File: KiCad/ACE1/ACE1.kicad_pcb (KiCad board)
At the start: 2 copper layers, 198.2 x 224.3 mm, 148 parts, among them IC1 78T, Q1 2N3904, Q2 2N2369, Q3 BC183, Q4 2N3904, X1 6.556MHz

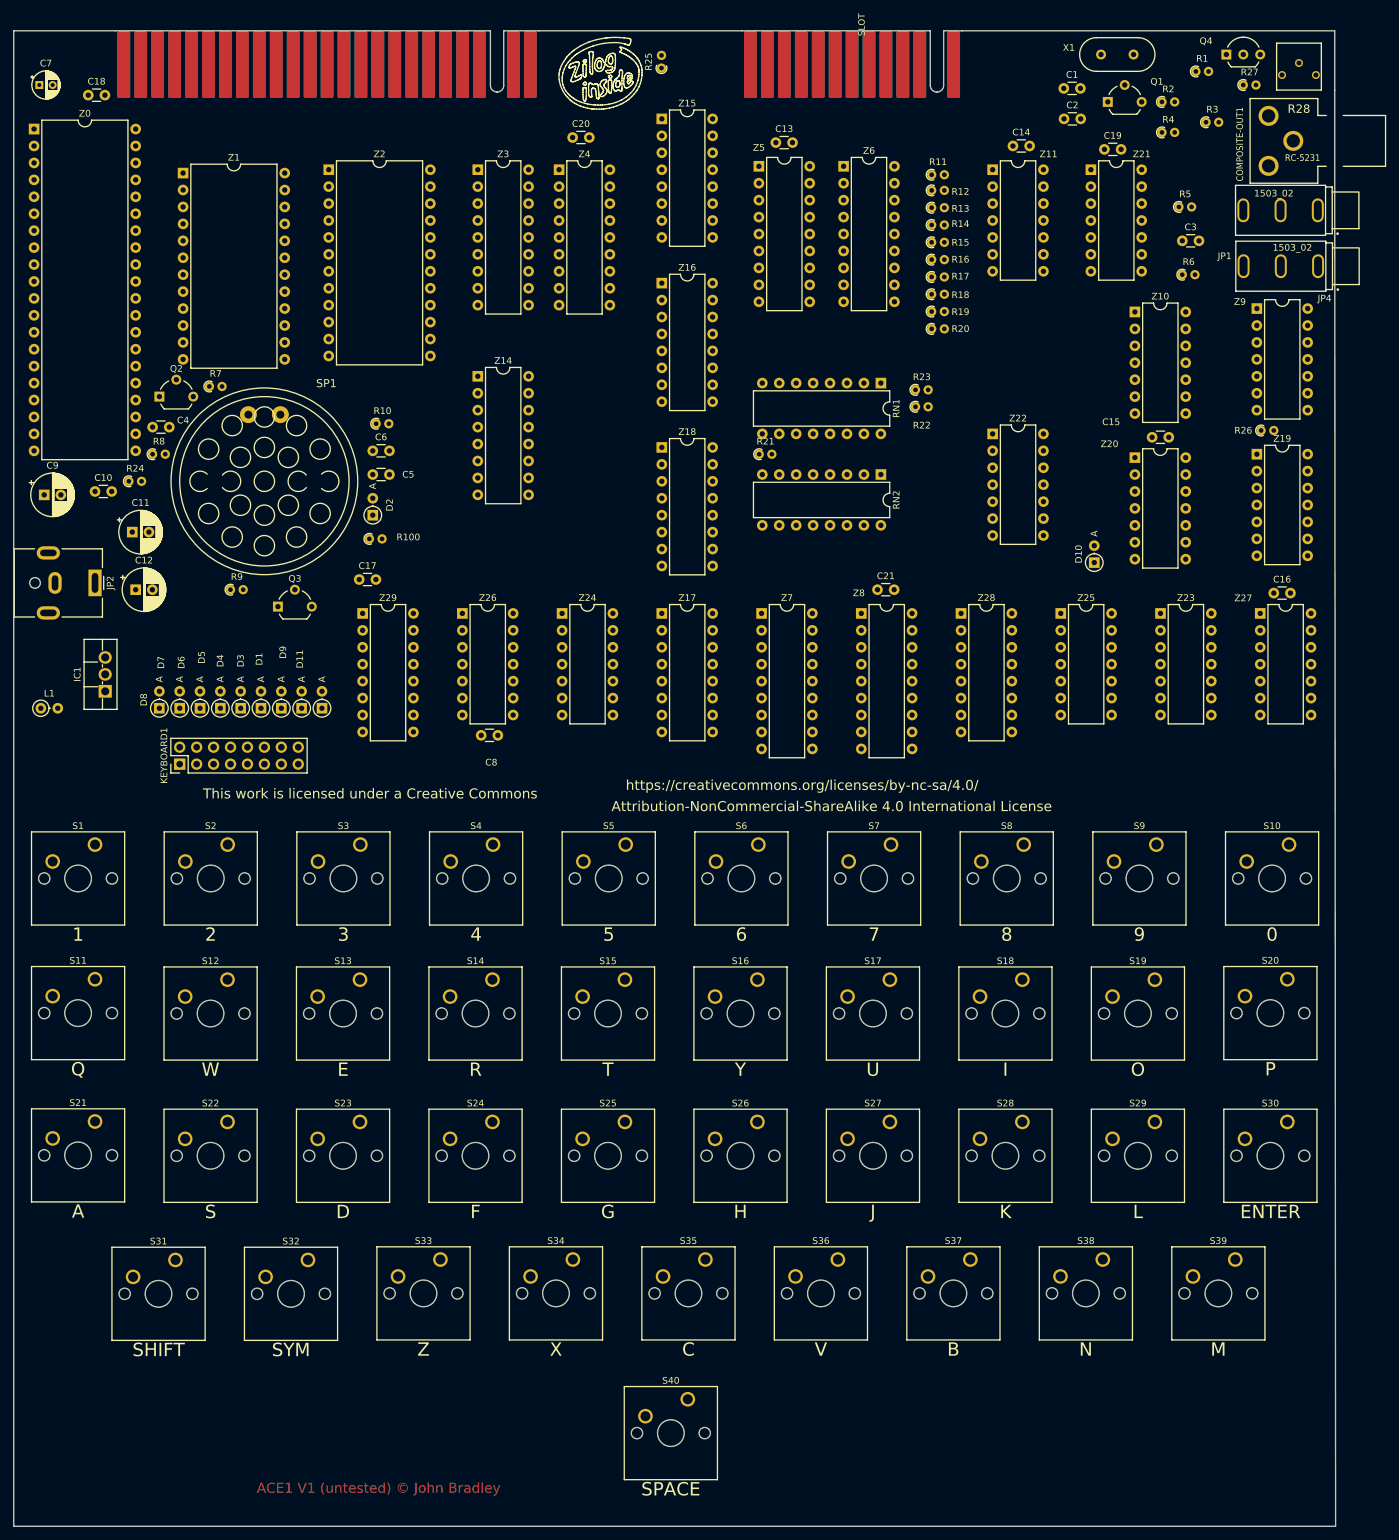
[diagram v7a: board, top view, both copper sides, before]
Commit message: Update Ace1 & ACE2 to new Keyboard Plug and add PCB routing.
Signed-off-by: John Bradley <flypie@rocketmail.com>
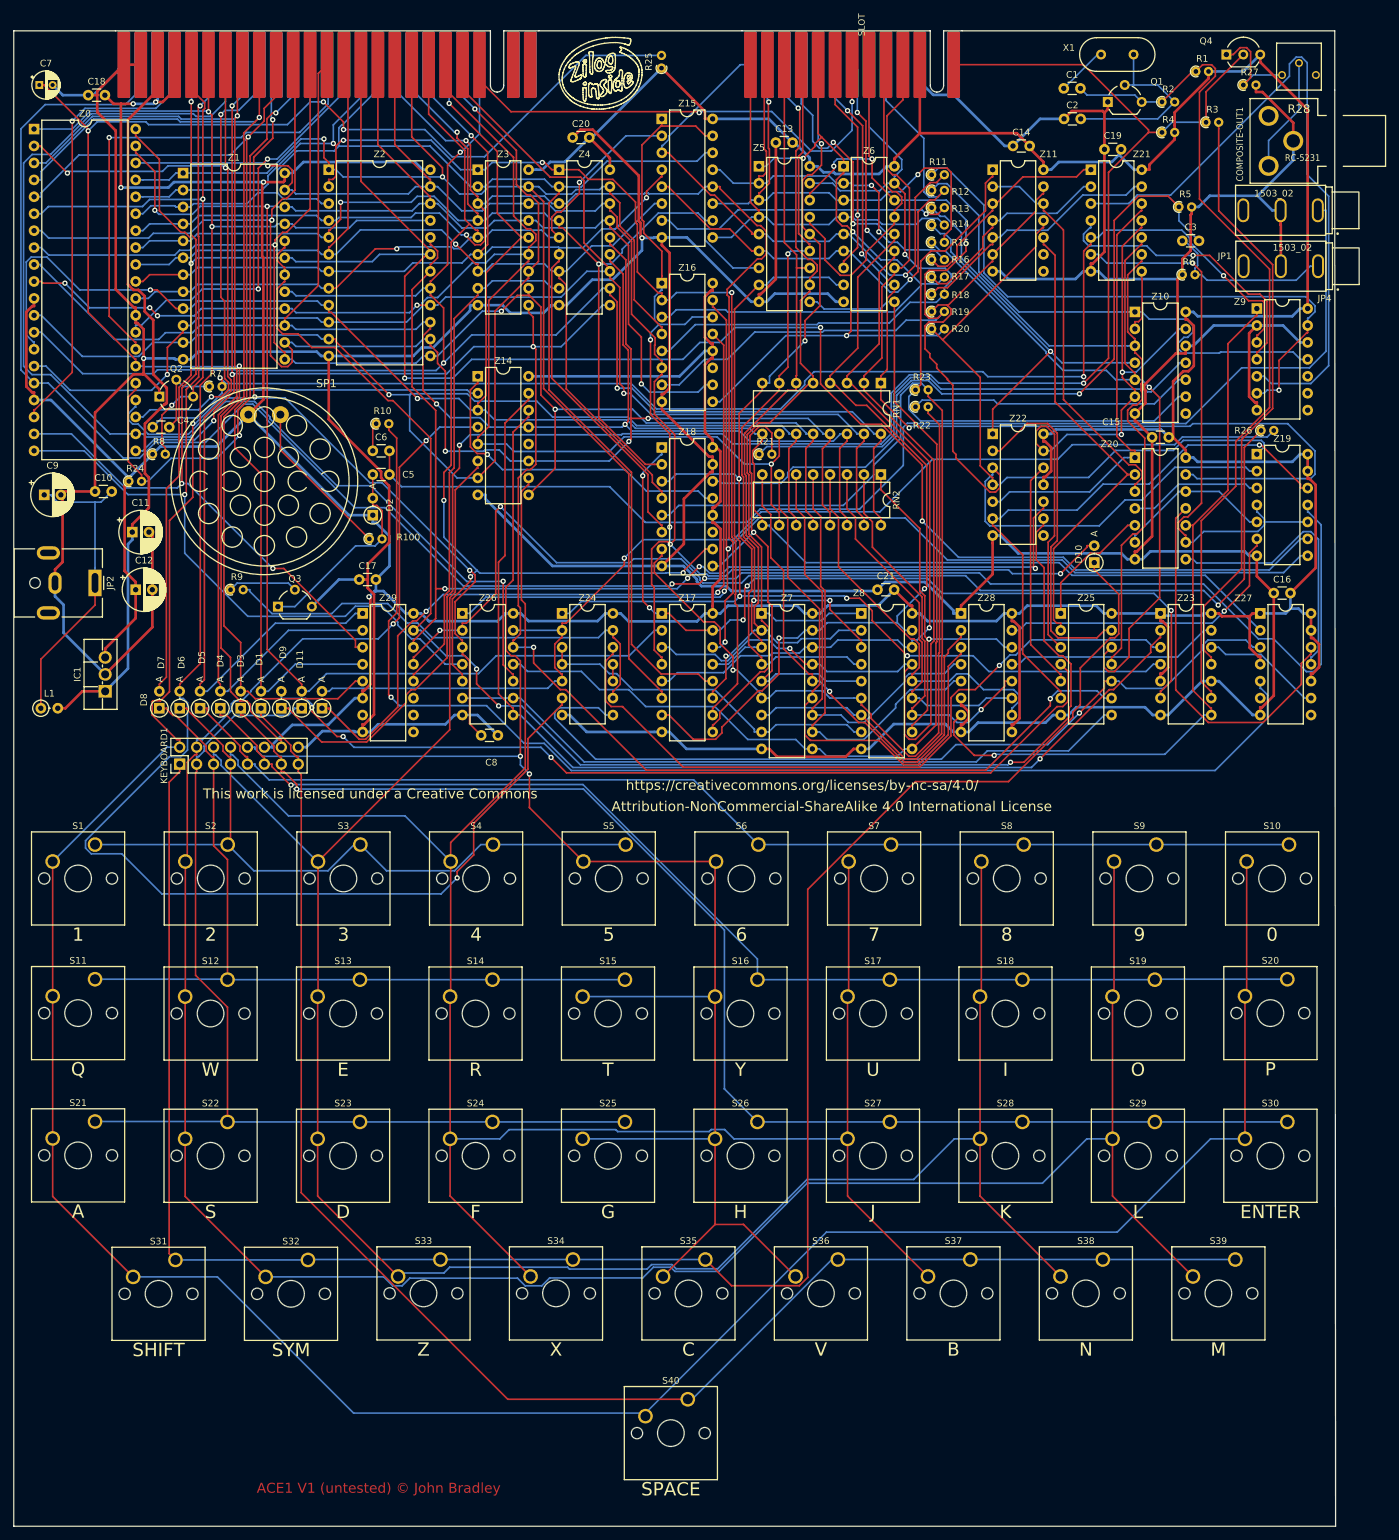
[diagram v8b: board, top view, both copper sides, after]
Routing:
- net GND: track 0.00 -> 1010.9 mm, vias 0 -> 2
- net VCC: track 0.00 -> 885.0 mm, vias 0 -> 5
- net /COLA: track 0.00 -> 426.5 mm, vias 0 -> 1
- net /COLB: track 0.00 -> 367.4 mm, vias 0 -> 2
- net /AD10: track 0.00 -> 346.0 mm, vias 0 -> 4
- net /COLC: track 0.00 -> 325.1 mm
- net /ROW8: track 0.00 -> 309.0 mm
- net /~{INT}: track 0.00 -> 307.8 mm, vias 0 -> 2
- net /COLD: track 0.00 -> 299.7 mm
- net /DA0: track 0.00 -> 293.4 mm, vias 0 -> 3
- net /~{WR}: track 0.00 -> 288.6 mm, vias 0 -> 6
- net /AD11: track 0.00 -> 281.9 mm, vias 0 -> 3
- net /AD9: track 0.00 -> 278.5 mm, vias 0 -> 3
- net /VIDEO: track 0.00 -> 265.9 mm, vias 0 -> 2
- net Net-(D11-A): track 0.00 -> 258.0 mm, vias 0 -> 3
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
